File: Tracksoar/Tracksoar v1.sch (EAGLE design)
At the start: 36 parts, among them IC2 74AHC1G125DBV, U1 ATMEGA328P, Y1 16MHZ

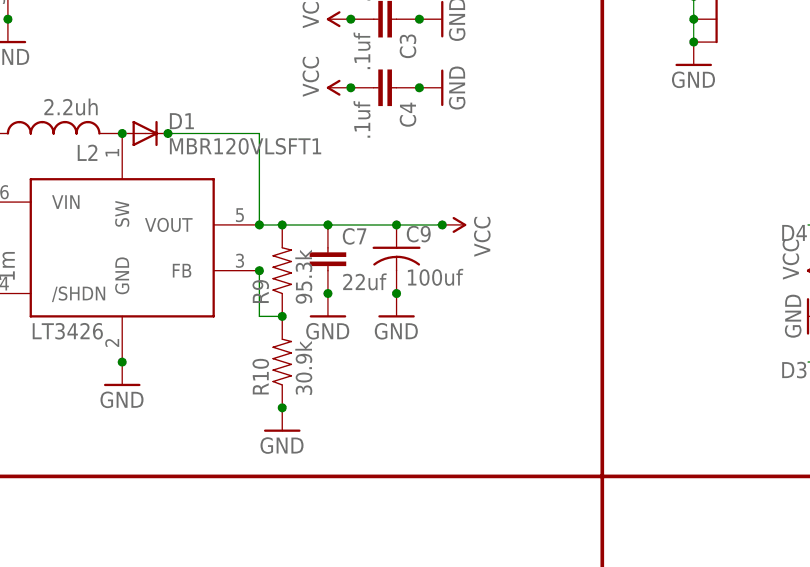
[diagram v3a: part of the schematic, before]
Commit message: removed components below gps
Removed the step up circuit components below the gps receiver and added
vias to prevent any interference
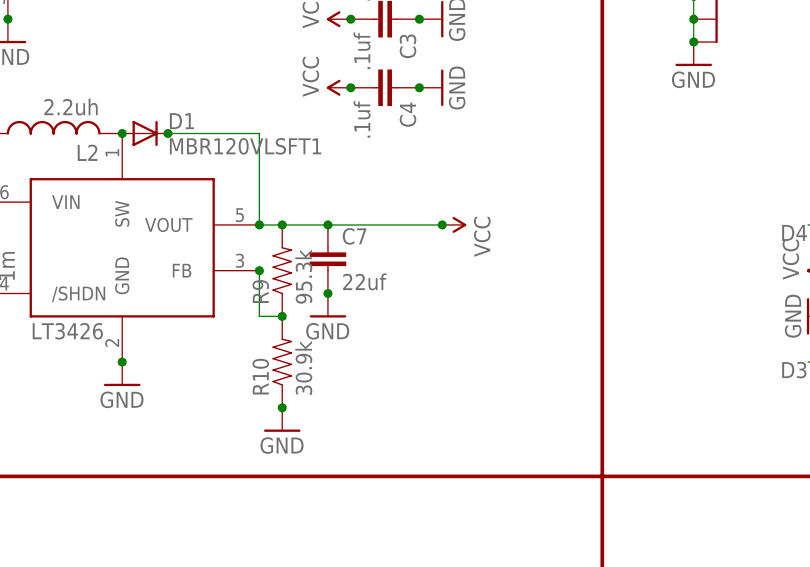
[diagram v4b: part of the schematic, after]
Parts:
- removed C9: 100uf, resistor:C-USC1206
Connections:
- net GND: no longer C9.2
- net VCC: no longer C9.1
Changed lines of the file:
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@@
 <part name="GND29" library="SparkFun-Aesthetics" deviceset="GND" device=""/>
 <part name="GND30" library="SparkFun-Aesthetics" deviceset="GND" device=""/>
-<part name="C9" library="resistor" deviceset="C-US" device="C1206" value="100uf"/>
-<part name="GND31" library="SparkFun-Aesthetics" deviceset="GND" device=""/>
 <part name="SHT21" library="sht21" deviceset="SHT21" device=""/>
 <part name="GPS-ANT" library="SparkFun-RF" deviceset="ANTENNA2" device="SMD3"/>
@@
 <instance part="GND29" gate="1" x="7.62" y="129.54"/>
 <instance part="GND30" gate="1" x="53.34" y="127"/>
-<instance part="C9" gate="G$1" x="60.96" y="134.62"/>
-<instance part="GND31" gate="1" x="60.96" y="127"/>
 <instance part="SHT21" gate="A" x="121.92" y="83.82"/>
 <instance part="GPS-ANT" gate="G$1" x="165.1" y="165.1" rot="R90"/>
@@
 </segment>
 <segment>
-<pinref part="C9" gate="G$1" pin="2"/>
-<pinref part="GND31" gate="1" pin="GND"/>
-<junction x="60.96" y="129.54"/>
-</segment>
-<segment>
 <pinref part="SHT21" gate="A" pin="VSS"/>
 <pinref part="GND20" gate="1" pin="GND"/>
@@
 <pinref part="LT3426" gate="G$1" pin="VOUT"/>
 <pinref part="SUPPLY1" gate="G$1" pin="VCC"/>
-<wire x1="66.04" y1="137.16" x2="60.96" y2="137.16" width="0.1524" layer="91"/>
 <pinref part="D1" gate="G$1" pin="C"/>
-<wire x1="60.96" y1="137.16" x2="53.34" y2="137.16" width="0.1524" layer="91"/>
+<wire x1="66.04" y1="137.16" x2="53.34" y2="137.16" width="0.1524" layer="91"/>
 <wire x1="53.34" y1="137.16" x2="48.26" y2="137.16" width="0.1524" layer="91"/>
 <wire x1="48.26" y1="137.16" x2="45.72" y2="137.16" width="0.1524" layer="91"/>
@@
 <junction x="53.34" y="137.16"/>
 <junction x="66.04" y="137.16"/>
-<pinref part="C9" gate="G$1" pin="1"/>
-<junction x="60.96" y="137.16"/>
 </segment>
 </net>
